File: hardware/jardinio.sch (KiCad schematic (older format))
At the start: 0 parts

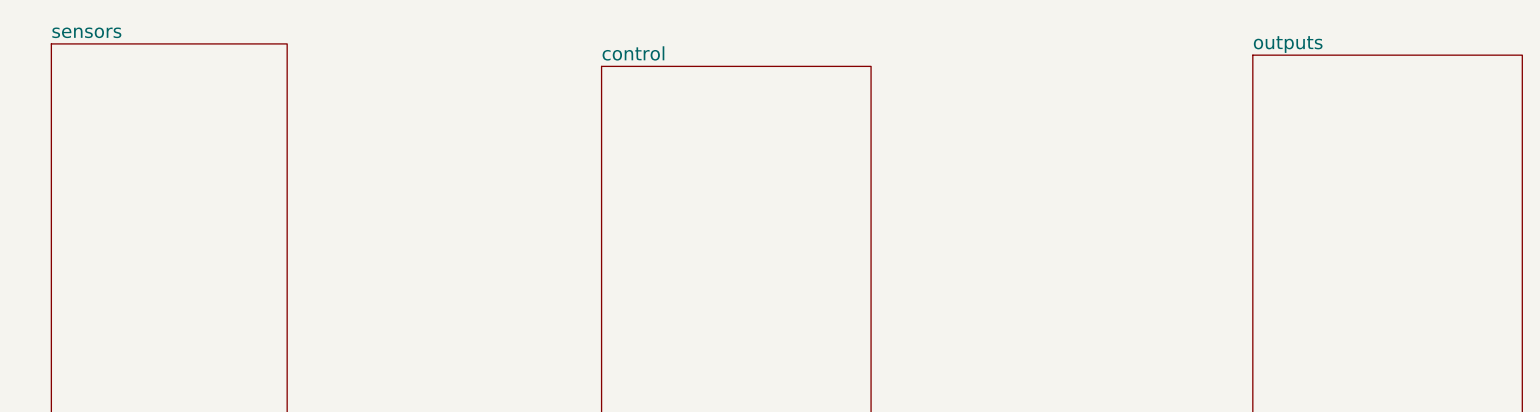
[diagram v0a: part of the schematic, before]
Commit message: sheets are named, global circuit is done.
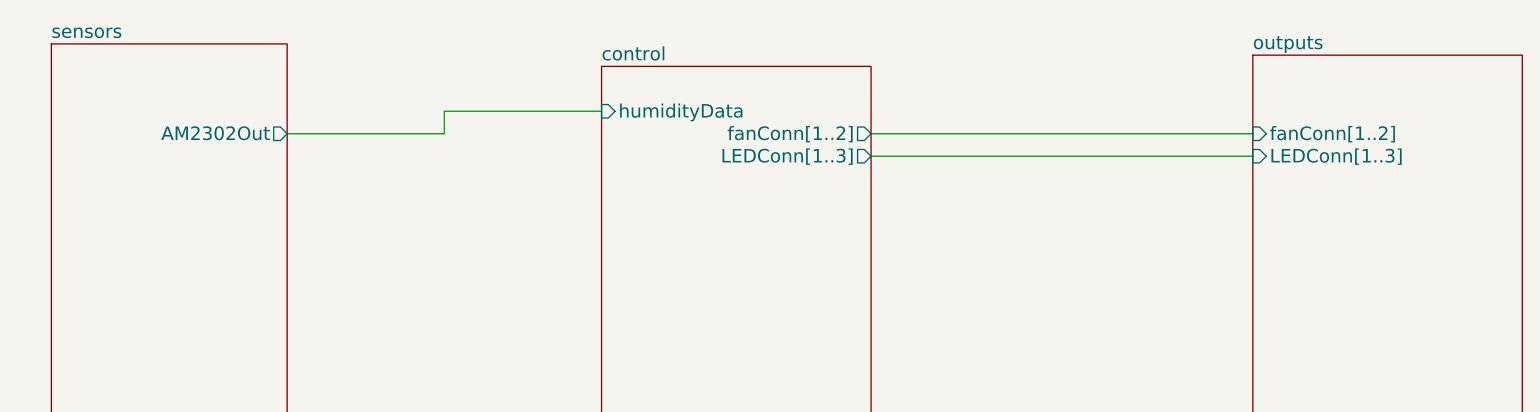
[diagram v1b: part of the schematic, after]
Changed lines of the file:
@@
 encoding utf-8
 Sheet 1 5
-Title ""
-Date ""
-Rev ""
-Comp ""
+Title "jardinIO circuit"
+Date "2018-04-18"
+Rev "0"
+Comp "Cedille"
 Comment1 ""
 Comment2 ""
@@
 F0 "control" 60
 F1 "control.sch" 60
+F2 "humidityData" I L 3350 1050 60
+F3 "LEDConn[1..3]" O R 4550 1250 60
+F4 "fanConn[1..2]" O R 4550 1150 60
 $EndSheet
 $Sheet
@@
 F0 "sensors" 60
 F1 "sensors.sch" 60
+F2 "AM2302Out" O R 1950 1150 60
 $EndSheet
 $Sheet
@@
 F0 "outputs" 60
 F1 "outputs.sch" 60
+F2 "LEDConn[1..3]" I L 6250 1250 60
+F3 "fanConn[1..2]" I L 6250 1150 60
 $EndSheet
+Wire Wire Line
+	6250 1150 4550 1150
+Wire Wire Line
+	6250 1250 4550 1250
+Wire Wire Line
+	3350 1050 2650 1050
+Wire Wire Line
+	2650 1050 2650 1150
+Wire Wire Line
+	2650 1150 1950 1150
 $EndSCHEMATC
